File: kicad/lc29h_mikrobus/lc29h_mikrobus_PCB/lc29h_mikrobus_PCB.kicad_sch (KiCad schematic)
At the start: 3 parts, among them IC1 MIKROE-924

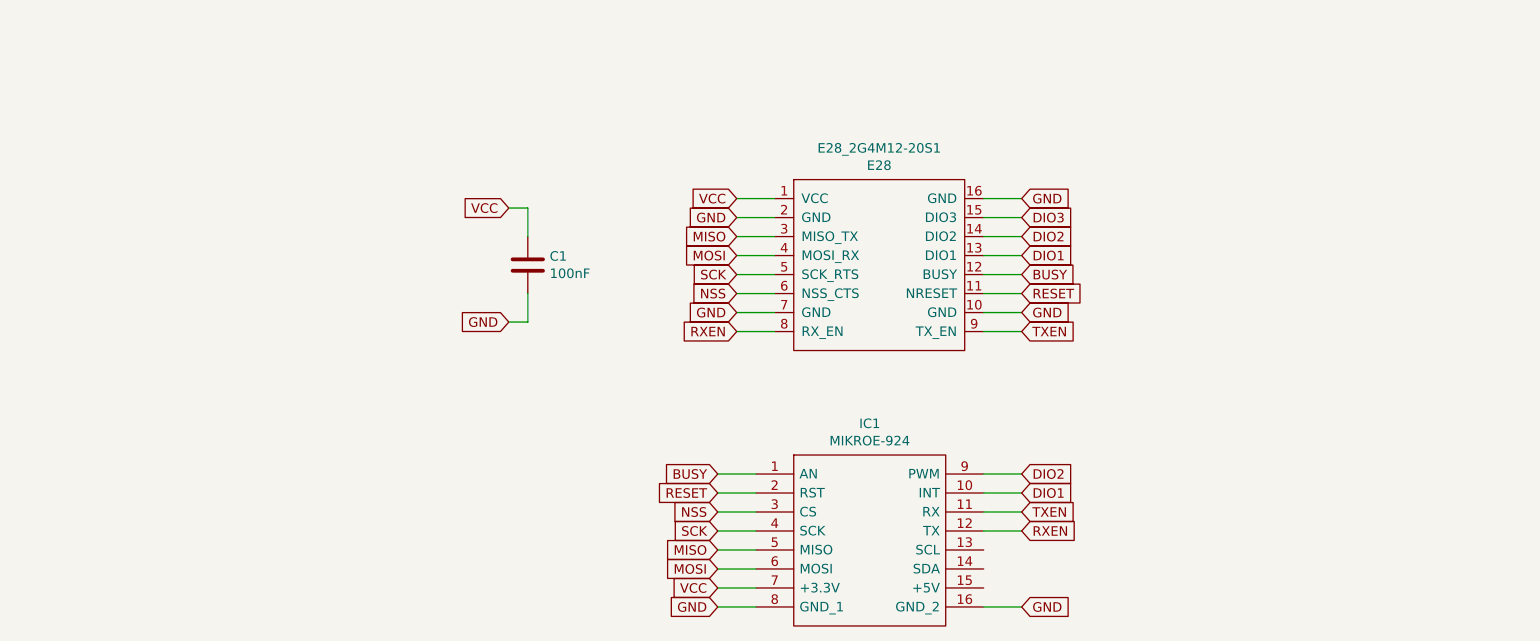
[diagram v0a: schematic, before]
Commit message: Ajout symboles/empreintes composants
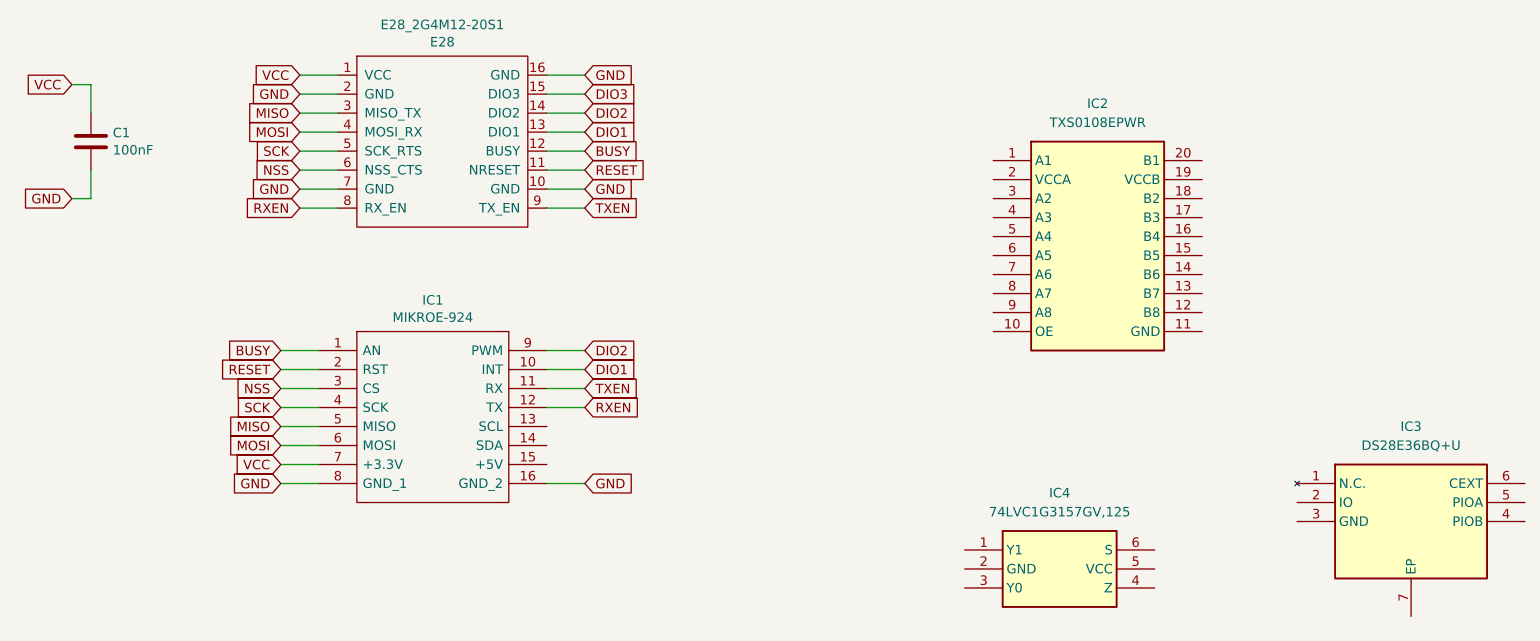
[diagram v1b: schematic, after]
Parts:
- added IC2: TXS0108EPWR, SOP65P640X120-20N, symbol TXS0108EPWR:TXS0108EPWR
- added IC3: DS28E36BQ+U, SON95P300X300X80-7N, symbol DS28E36BQ+U:DS28E36BQ+U
- added IC4: 74LVC1G3157GV,125, SOP95P275X110-6N, symbol 74LVC1G3157GV_125:74LVC1G3157GV,125
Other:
- moved on the sheet: C1, E28_2G4M12-20S1, IC1

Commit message: Début circuit
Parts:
- removed IC2: TXS0108EPWR, SOP65P640X120-20N, symbol TXS0108EPWR:TXS0108EPWR
- added C2: 0.47u, symbol Device:C
- added Q1: BSS123L, SOT96P237X111-3N, symbol BSS123L:BSS123L
- added R1: 1k, symbol Device:R
- added R2: 10k, symbol Device:R
- added R3: 3.3k, symbol Device:R
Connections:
- net GND: now also IC3.3 (GND), IC4.2 (GND), C2.2
- net VCC: now also IC3.6 (CEXT), IC4.5 (VCC), C2.1, Q1.1 (G), R1.1, R2.1, R3.1
- net at IC4.6 (S): now also R2.2
- net at IC3.1 (N.C.): now also R1.2
- new net: Q1.3 (D), R3.2
- no-connect marks 0 -> 2
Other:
- moved on the sheet: C1, E28_2G4M12-20S1, IC1, IC3, IC4

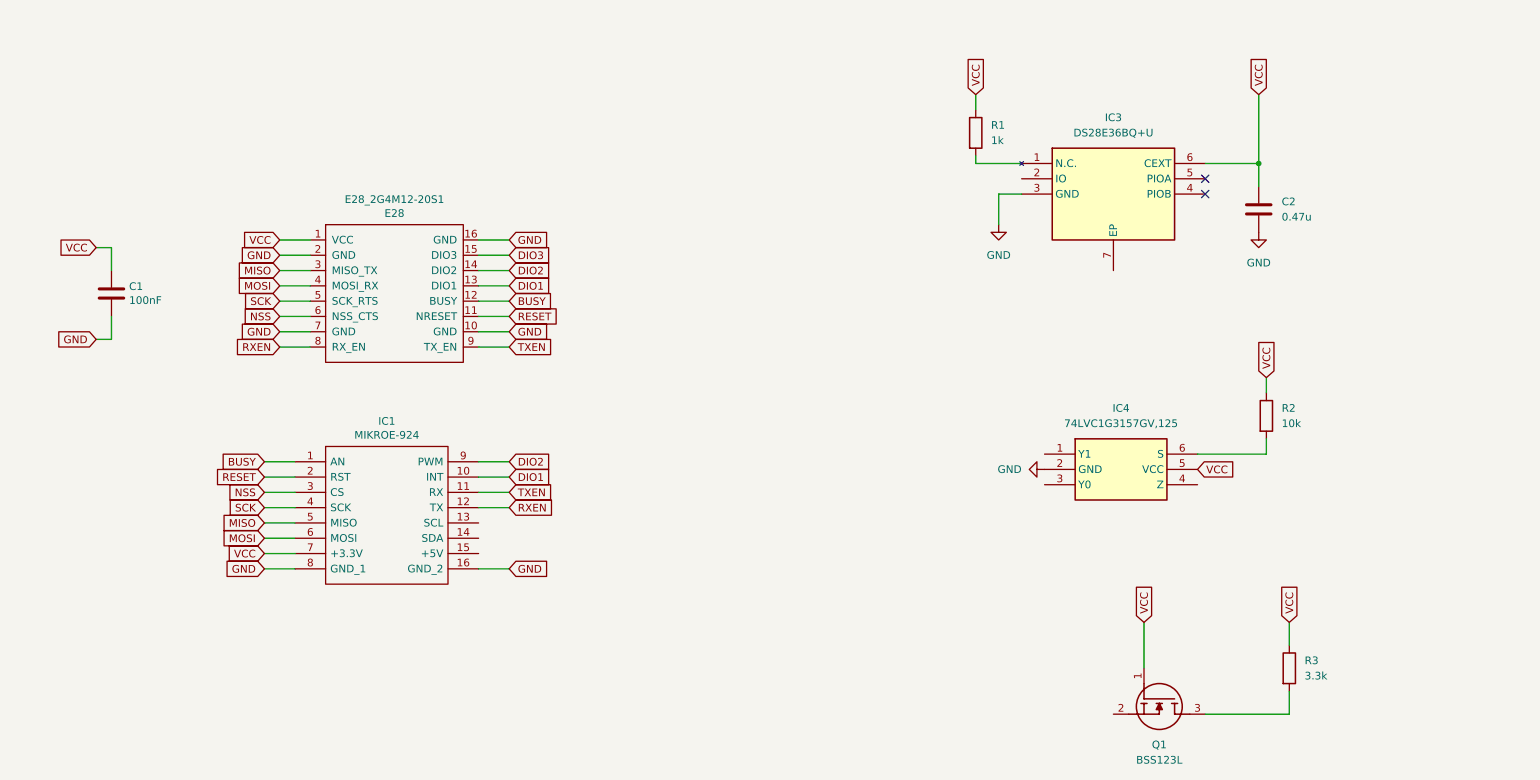
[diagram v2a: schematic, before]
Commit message: ajout level shifter pour le module GNSS
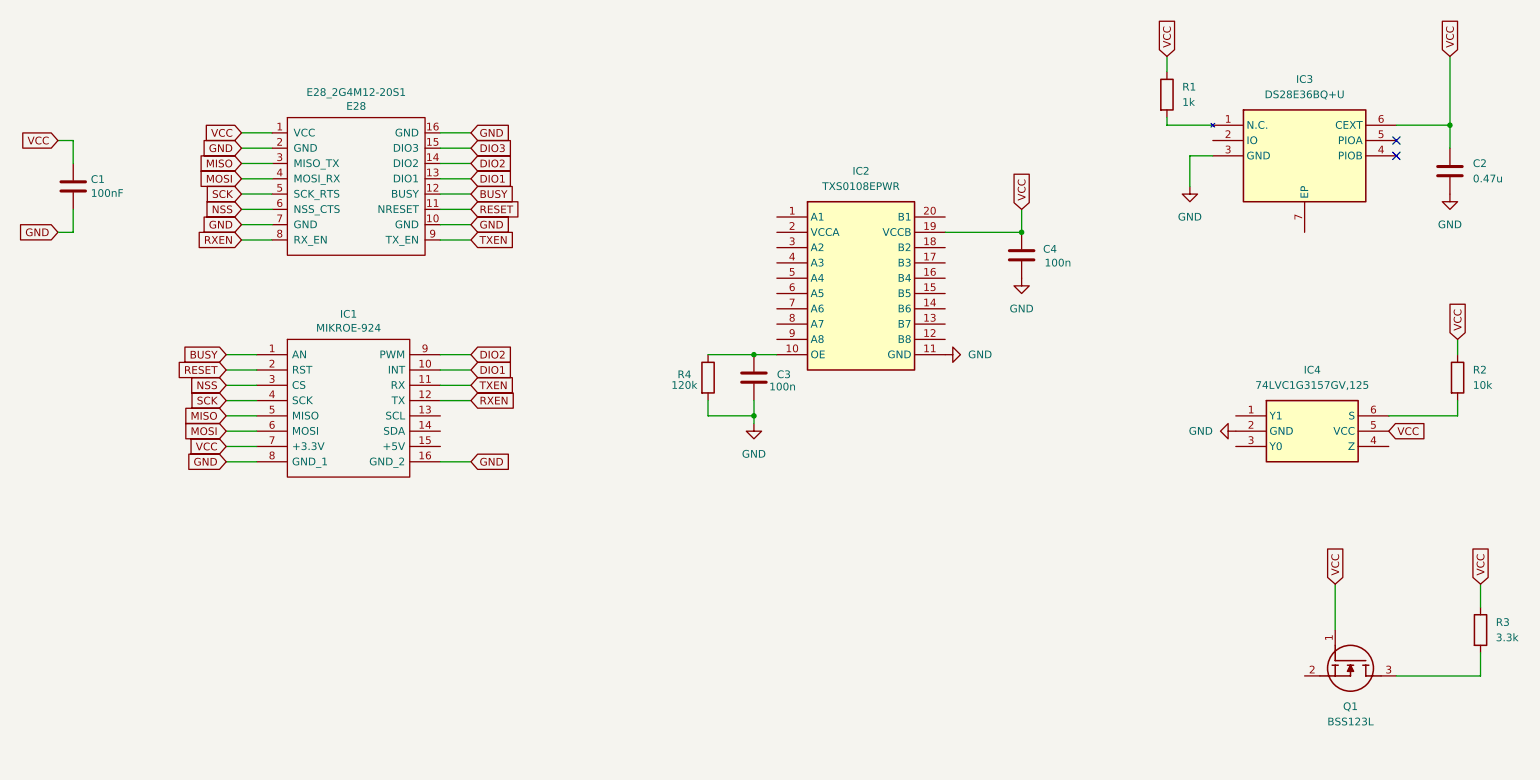
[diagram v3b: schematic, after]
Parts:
- added C3, C4: 100n, symbol Device:C
- added IC2: TXS0108EPWR, SOP65P640X120-20N, symbol TXS0108EPWR:TXS0108EPWR
- added R4: 120k, symbol Device:R
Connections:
- net GND: now also C3.2, C4.2, IC2.11 (GND), R4.2
- net VCC: now also C4.1, IC2.19 (VCCB)
- new net: C3.1, IC2.10 (OE), R4.1
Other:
- moved on the sheet: C1, C2, E28_2G4M12-20S1, IC1, IC3, IC4, Q1, R1, R2, R3

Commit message: schematic module gnss, clickID et voltage translator
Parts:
- removed C1: 100nF, Capacitor_SMD:C_0805_2012Metric_Pad1.18x1.45mm_HandSolder, symbol Device:C
- removed C2: 0.47u, symbol Device:C
- removed C3, C4: 100n, symbol Device:C
- removed E28_2G4M12-20S1: E28, LIB_E28-2G4M12-20S:E28-2G4M12-20S, symbol Lib_E28-2G4M12-20S:E28
- removed IC2: TXS0108EPWR, SOP65P640X120-20N, symbol TXS0108EPWR:TXS0108EPWR
- removed IC3: DS28E36BQ+U, SON95P300X300X80-7N, symbol DS28E36BQ+U:DS28E36BQ+U
- removed IC4: 74LVC1G3157GV,125, SOP95P275X110-6N, symbol 74LVC1G3157GV_125:74LVC1G3157GV,125
- removed Q1: BSS123L, SOT96P237X111-3N, symbol BSS123L:BSS123L
- removed R1: 1k, symbol Device:R
- removed R2: 10k, symbol Device:R
- removed R3: 3.3k, symbol Device:R
- removed R4: 120k, symbol Device:R
- added BT101: 3000TR, 3000TR, symbol 3000TR:3000TR
- added C101: 4.7u, symbol Device:C
- added C102, C105, C106: 100n, symbol Device:C
- added C103: 33p, symbol Device:C
- added C104: 0.47u, symbol Device:C
- added D101: LED, symbol Device:LED
- added D102: ESDARF02-1BU2CK, ESDARF021BU2CK, symbol ESDARF02-1BU2CK:ESDARF02-1BU2CK
- added IC101: DS28E36BQ+U, SON95P300X300X80-7N, symbol DS28E36BQ+U:DS28E36BQ+U
- added IC102: 74LVC1G3157GV,125, SOP95P275X110-6N, symbol 74LVC1G3157GV_125:74LVC1G3157GV,125
- added IC103: TXS0102DQER, SON35P100X140X40-8N, symbol TXS0102DQER:TXS0102DQER
- added Q101: BC856B-13-F, SOT96P240X110-3N, symbol BC856B-13-F:BC856B-13-F
- added Q102: BSS123L, SOT96P237X111-3N, symbol BSS123L:BSS123L
- added R101: 39k, symbol Device:R
- added R102: 470, symbol Device:R
- added R103: 0, symbol Device:R
- added R104, R107, R114, R115: 1k, symbol Device:R
- added R105: 2.2k, symbol Device:R
- added R106: 3.3k, symbol Device:R
- added R108: 10k, symbol Device:R
- added R109: 120k, symbol Device:R
- added R110, R111, R112, R113: 4.7k, symbol Device:R
- added SW101: SW_Nidec_CAS-120A1, Button_Switch_SMD:Nidec_Copal_CAS-120A, symbol Switch:SW_Nidec_CAS-120A1
- added U101: ~, symbol LC29H:LC29H
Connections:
- net GND: now also C101.2, C102.2, C103.2, C104.2, C105.2, C106.2, D101.1 (K), IC101.3 (GND), IC101.7 (EP), IC102.2 (GND), IC103.4 (GND), Q101.2 (E), R109.2, U101.10 (GND), U101.12 (GND), U101.13 (GND), U101.24 (GND)
- net VCC: now also C104.1, C106.1, IC101.6 (CEXT), IC102.5 (VCC), IC103.8 (VCCB), Q102.1 (G), R103.1, R104.2, R106.2, R107.1, R108.1, R112.1, R113.1, U101.23 (VCC)
- net SCL: now reaches IC1.13 (SCL)
- net SCL: now also IC103.7 (B1), R112.2
- net SDA: now reaches IC1.14 (SDA)
- net SDA: now also IC103.6 (B2), R113.2
- net BUSY: no longer names the net of IC1.1 (AN)
- net DIO1 renamed 1PPS
- net 1PPS: now also U101.3 (1PPS)
- net DIO2 renamed WUP
- net WUP: now also U101.1 (WAKE_UP)
- net MISO: no longer names the net of IC1.5 (MISO)
- net MOSI: no longer names the net of IC1.6 (MOSI)
- net NSS renamed CE_HOST
- net CE_HOST: now also IC102.4 (Z)
- net RESET renamed RST
- net RST: now also IC102.6 (S), R105.1, R108.2
- net RXEN renamed TX1
- net TX1: now also U101.20 (TXD1/SPI_MISO)
- net SCK: no longer names the net of IC1.4 (SCK)
- net TXEN renamed RX1
- net RX1: now also U101.21 (RXD1/SPI_MOSI)
- new net: R101.2, SW101.1 (C)
- new net: SW101.2 (B), U101.5 (D_SEL1), U101.6 (D_SEL2)
- new net: R102.1, R103.2
- new net: R115.1, U101.15 (TXD2)
- new net: IC101.2 (IO), Q102.2 (S), R107.2
- new net: D101.2 (A), R102.2
- new net: Q101.1 (B), R105.2
- new net: Q101.3 (C), U101.8 (RESET_N)
- new net: IC102.3 (Y0), Q102.3 (D), R106.1
- new net: R114.1, U101.16 (RXD2)
- new net ANT_ON: U101.14 (ANT_ON)
- new net CE: IC102.1 (Y1)
- new net VBCK: C101.1, C102.1, C103.1, U101.22 (V_BCKP)
- new net VDD_EXT: C105.1, IC103.1 (VCCA), IC103.5 (OE), R101.1, R109.1, R110.1, R111.1, U101.7 (VDD_EXT)
- new net VDD_RF: U101.9 (VDD_RF)
- new net mSCL: IC103.2 (A1), R111.2, U101.19 (I2C_SCL/SPI_CLK)
- new net mSDA: IC103.3 (A2), R110.2, U101.18 (I2C_SDA/SPI_CS)
- no-connect marks 2 -> 10
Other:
- moved on the sheet: IC1

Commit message: signaux ant_on, rf_in, vdd_rf
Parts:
- added C1, C3: 100p, symbol Device:C
- added C2: 100n, symbol Device:C
- added J1: Conn_Coaxial, symbol Connector:Conn_Coaxial
- added L1: 68n, symbol Device:L
- added Q1: DMP3013SFV, Package_SON:Diodes_PowerDI3333-8, symbol Transistor_FET:DMP3013SFV
- added Q2: NPN, symbol Simulation_SPICE:NPN
- added R1: 10, symbol Device:R
- added R2: 10k, symbol Device:R
- added R3, R4: R, symbol Device:R
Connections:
- net ANT_ON: now also R3.1
- net GND: now also D102.1, C2.2, C3.2, J1.2 (Ext), Q2.3 (E), R4.2
- net VDD_RF: now also Q1.1 (S), Q1.2 (S), Q1.3 (S), R2.1
- net at D102.2: now also C1.1, J1.1 (In), L1.2
- net RF_IN: now reaches U101.11 (RF_IN)
- net RF_IN: now also C1.2
- new net: Q1.4 (G), Q2.1 (C), R2.2
- new net: Q1.5 (D), R1.1
- new net: C2.1, C3.1, L1.1, R1.2
- new net: Q2.2 (B), R3.2, R4.1
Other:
- moved on the sheet: D102

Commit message: Ajout empreinte PCB
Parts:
- U101: value ~ -> LC29H; footprint (none) -> LC29H:LC29HEA
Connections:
- net RX1: now also IC1.12 (TX); no longer IC1.11 (RX)
- net TX1: now also IC1.11 (RX); no longer IC1.12 (TX)
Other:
- moved on the sheet: BT101
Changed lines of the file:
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@@
 		)
 	)
-	(global_label "RX1"
-		(shape output)
-		(at 80.01 41.91 0)
-		(effects
-			(font
-				(size 1.27 1.27)
-			)
-			(justify left)
-		)
-		(property "Intersheetrefs" "${INTERSHEET_REFS}"
-			(at 80.01 41.91 0)
-			(effects
-				(font
-					(size 1.27 1.27)
-				)
-				(hide yes)
-			)
-		)
-	)
 	(global_label "mSCL"
 		(shape bidirectional)
@@
 		)
 	)
+	(global_label "RX1"
+		(shape output)
+		(at 80.01 44.45 0)
+		(effects
+			(font
+				(size 1.27 1.27)
+			)
+			(justify left)
+		)
+		(property "Intersheetrefs" "${INTERSHEET_REFS}"
+			(at 80.01 44.45 0)
+			(effects
+				(font
+					(size 1.27 1.27)
+				)
+				(hide yes)
+			)
+		)
+	)
 	(global_label "CE_HOST"
 		(shape bidirectional)
@@
 		)
 	)
-	(global_label "TX1"
-		(shape input)
-		(at 80.01 44.45 0)
-		(effects
-			(font
-				(size 1.27 1.27)
-			)
-			(justify left)
-		)
-		(property "Intersheetrefs" "${INTERSHEET_REFS}"
-			(at 80.01 44.45 0)
-			(effects
-				(font
-					(size 1.27 1.27)
-				)
-				(hide yes)
-			)
-		)
-	)
 	(global_label "RST"
 		(shape bidirectional)
@@
 		)
 	)
+	(global_label "TX1"
+		(shape input)
+		(at 80.01 41.91 0)
+		(effects
+			(font
+				(size 1.27 1.27)
+			)
+			(justify left)
+		)
+		(property "Intersheetrefs" "${INTERSHEET_REFS}"
+			(at 80.01 41.91 0)
+			(effects
+				(font
+					(size 1.27 1.27)
+				)
+				(hide yes)
+			)
+		)
+	)
 	(global_label "VCC"
 		(shape input)
@@
 	(symbol
 		(lib_id "3000TR:3000TR")
-		(at 275.59 170.18 270)
+		(at 270.51 160.02 270)
 		(unit 1)
 		(exclude_from_sim no)
@@
 		(fields_autoplaced yes)
 		(property "Reference" "BT101"
-			(at 279.4 180.3399 90)
+			(at 274.32 170.1799 90)
 			(effects
 				(font
@@
 		)
 		(property "Value" "3000TR"
-			(at 279.4 182.8799 90)
+			(at 274.32 172.7199 90)
 			(effects
 				(font
@@
 		)
 		(property "Footprint" "3000TR"
-			(at 180.67 189.23 0)
+			(at 175.59 179.07 0)
 			(effects
 				(font
@@
 		)
 		(property "Datasheet" "https://www.keyelco.com/produchttps://www.mouser.co.za/datasheet/2/215/3000TR-742873.pdft-pdf.cfm?p=777"
-			(at 80.67 189.23 0)
+			(at 75.59 179.07 0)
 			(effects
 				(font
@@
 		)
 		(property "Description" "Battery Retainer Coin, 12.0mm 1 Cell SMD (SMT) Tab"
-			(at 275.59 170.18 0)
+			(at 270.51 160.02 0)
 			(effects
 				(font
@@
 		)
 		(property "Height" "3.43"
-			(at -119.33 189.23 0)
+			(at -124.41 179.07 0)
 			(effects
 				(font
@@
 		)
 		(property "Manufacturer_Name" "Keystone Electronics"
-			(at -219.33 189.23 0)
+			(at -224.41 179.07 0)
 			(effects
 				(font
@@
 		)
 		(property "Manufacturer_Part_Number" "3000TR"
-			(at -319.33 189.23 0)
+			(at -324.41 179.07 0)
 			(effects
 				(font
@@
 		)
 		(property "Mouser Part Number" "534-3000TR"
-			(at -419.33 189.23 0)
+			(at -424.41 179.07 0)
 			(effects
 				(font
@@
 		)
 		(property "Mouser Price/Stock" "https://www.mouser.co.uk/ProductDetail/Keystone-Electronics/3000TR?qs=811De8TLL%252BeRUCmGL5ZsKg%3D%3D"
-			(at -519.33 189.23 0)
+			(at -524.41 179.07 0)
 			(effects
 				(font
@@
 		)
 		(property "Arrow Part Number" "3000TR"
-			(at -619.33 189.23 0)
+			(at -624.41 179.07 0)
 			(effects
 				(font
@@
 		)
 		(property "Arrow Price/Stock" "https://www.arrow.com/en/products/3000tr/keystone-electronics"
-			(at -719.33 189.23 0)
+			(at -724.41 179.07 0)
 			(effects
 				(font
@@
 			)
 		)
-		(property "Value" "~"
+		(property "Value" "LC29H"
 			(at 313.055 35.56 0)
 			(effects
@@
 			)
 		)
-		(property "Footprint" ""
+		(property "Footprint" "LC29H:LC29HEA"
 			(at 313.69 54.61 0)
 			(effects
